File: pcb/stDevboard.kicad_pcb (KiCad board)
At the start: 4 copper layers, 50 x 100 mm, 165 parts, among them IC1 MPM3610GQV-Z, IC2 IRFR9014PBF, IC3 ICM-45686, IC4 ICM-45686, IC5 MMC5983MA, IC6 AT25SF041B-SSHB-B, IC7 IRFR9014PBF, J1 USB_C_Receptacle_USB2.0_16P, J10 Micro_SD_Card_Det2, J2 USB_C_Receptacle_USB2.0_16P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

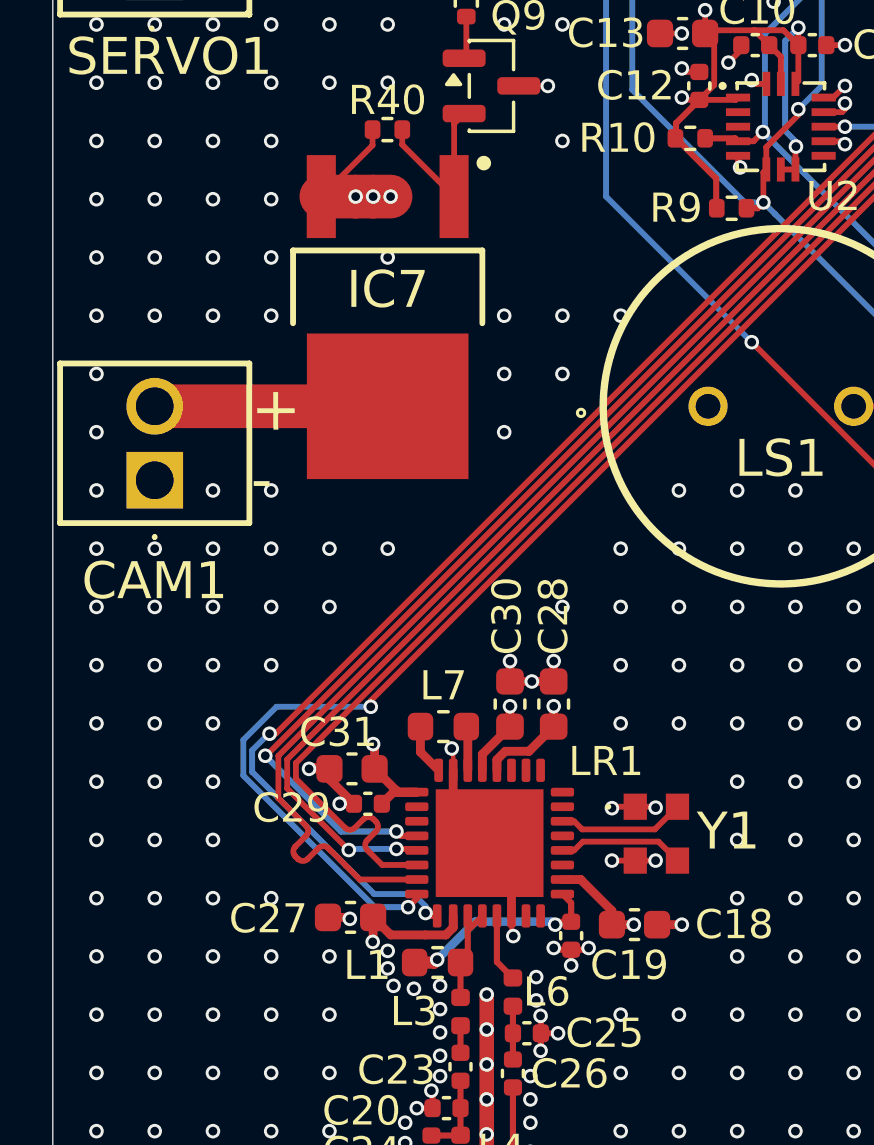
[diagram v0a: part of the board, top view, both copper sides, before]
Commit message: fixed vr_pa trace impedance (thanks mpk)
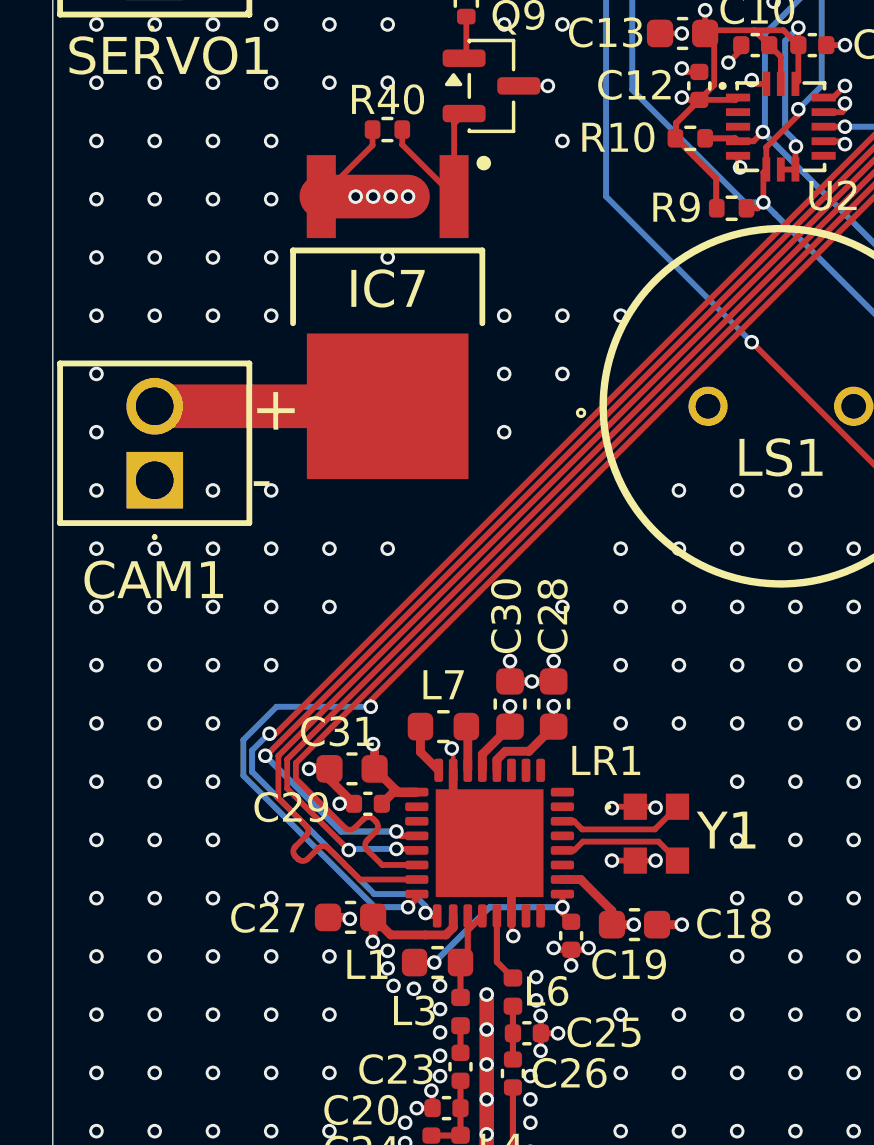
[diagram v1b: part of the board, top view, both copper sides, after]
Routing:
- net +BATT: track 114.4 -> 115.0 mm, vias 5 -> 6

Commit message: added silkscreen art and credits
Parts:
- added G***: LOGO, footprints:logo, B.Cu at (134.0, 172.0)
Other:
- board text added: "IRIS"
- board text added: "This board would not exist without mpk's help on rf. Thanks to everyone in Hack Club for supporting me on this journey."
- board text added: "by tty7 v1.0"
